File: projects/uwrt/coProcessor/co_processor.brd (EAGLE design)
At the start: 101.6 x 101.6 mm, 64 parts, among them U1 MPU-9250, U3 HTU21D

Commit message: No frills processing board revision 1.0.0
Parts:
- removed C1, C2: 0.1uF, rcl:C025-025X050
- removed C3: 10nF, rcl:C025-025X050
- removed C4: 100uF, rcl:C025-025X050
- removed C5: 4.7uF, rcl:C025-025X050
- removed C6: 100nF, rcl:C025-025X050
- removed JTAG_HEADER: M05X2-50MIL_SHROUD, Connectors:M05X2-50MIL-SHROUD
- removed U$2: LPS25H, st-microelectronics:LPS25H
- removed U$3: 24AA02, microchip:SO-08M
- removed U1: MPU-9250, SparkFun-Sensors:QFN24-3X3
- removed U3: HTU21D, SparkFun-Sensors:DFN-6-3X3-HTU21D
- added HB_R, HB_R1: 330, SparkFun-Resistors:0603
- added JTAG: (no value), pinhead:2X10
- added MICROSD: MICRO-SD_CARD_SOCKET, SparkFun-Connectors:MICRO-SD-SOCKET
- added MINI_USB_B: USB_MINI-B_SMT, SparkFun-Connectors:USB-MINIB
- added OSC1_C: 1nF, capacitor-wima:C2.5-2
- added OSC2_C: 1 nF, capacitor-wima:C2.5-2
- added Q1: (no value), crystal:HC49/S
- added RESET_SWITCH: (no value), switch-omron:B3F-10XX
- added STATUS_1, STATUS_2: (no value), SparkFun-LED:LED-1206
- added SWITCHES: 39-30-1040, molex:5569-04A2
- moved C15 300.6 mm to (70.6, 30.2), turned to 270 degrees
- moved C14 286.5 mm to (66.7, 30.2), turned to 270 degrees
- moved PWM_R9 278.5 mm to (72.2, 95.2), turned to 90 degrees
- moved PWM_LED9 275.8 mm to (70.6, 97.6), turned to 90 degrees
- moved C13 272.5 mm to (62.7, 30.2), turned to 270 degrees
- moved PWM_R8 269.0 mm to (68.3, 95.2), turned to 90 degrees
- moved PWM_LED8 266.3 mm to (66.7, 97.6), turned to 90 degrees
- moved PWM_R7 259.5 mm to (64.3, 95.2), turned to 90 degrees
- moved C12 258.5 mm to (58.7, 30.2), turned to 270 degrees
- moved PWM_LED7 256.8 mm to (62.7, 97.6), turned to 90 degrees
- moved PWM_R6 250.1 mm to (60.3, 95.2), turned to 90 degrees
- moved PWM_LED6 247.4 mm to (58.7, 97.6), turned to 90 degrees
- moved C11 244.4 mm to (54.8, 30.2), turned to 270 degrees
- moved PWM_R5 240.6 mm to (56.4, 95.2), turned to 90 degrees
- moved PWM_LED5 237.9 mm to (54.8, 97.6), turned to 90 degrees
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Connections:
- removed net GND1: JTAG_HEADER.3, JTAG_HEADER.5, JTAG_HEADER.9
- removed net N$6: U1.18, U1.20
- removed net N$9: C1.1, U1.10
- removed net TCK: JTAG_HEADER.4
- removed net TMS: JTAG_HEADER.2
- removed net VCC: JTAG_HEADER.1
- new net GND_ESC: PWM.1, PWM1.1, PWM2.1, PWM3.1, PWM4.1, PWM5.1, PWM6.1, PWM7.1, PWM8.1, PWM9.1, PWM_LED.C, PWM_LED1.C, PWM_LED2.C, PWM_LED3.C, PWM_LED4.C, PWM_LED5.C, PWM_LED6.C, PWM_LED7.C, PWM_LED8.C, PWM_LED9.C
- new net HB_OUT: HB_R.1, STM32F405.38
- new net HB_OUT1: HB_R1.1, STM32F405.37
- new net JTAG_RST: JTAG.3, STM32F405.56
- new net JTAG_TCK: JTAG.9, STM32F405.49
- new net JTAG_TDI: JTAG.5, STM32F405.50
- new net JTAG_TDO: JTAG.13, STM32F405.55
- new net JTAG_TMS: JTAG.7, STM32F405.46
- new net KILL_SW: STM32F405.34, SWITCHES.3
- new net N$3: HB_R1.2, STATUS_2.A
- new net NRST: JTAG.15, RESET_SWITCH.3, RESET_SWITCH.4, STM32F405.7
- new net OSC_IN: OSC1_C.2, Q1.1, STM32F405.5
- new net OSC_OUT: OSC2_C.2, Q1.2, STM32F405.6
- new net SDIO_CK: MICROSD.SCLK, STM32F405.53
- new net SDIO_CMD: MICROSD.CS, STM32F405.54
- new net SDIO_D0: MICROSD.DO, STM32F405.39
- new net START_SW: STM32F405.33, SWITCHES.4
- new net USB_DM: MINI_USB_B.D-, STM32F405.36
- new net USB_DP: MINI_USB_B.D+, STM32F405.35
- net +3V3: now also C11.1, JTAG.1, JTAG.2, MICROSD.VCC, MINI_USB_B.VBUS, SWITCHES.1, SWITCHES.2; no longer C2.1, C3.1, C4.1, C5.1, C6.1, U$2.1, U$2.10, U1.1, U1.13, U1.8, U3.VDD
- net GND: now also JTAG.10, JTAG.12, JTAG.14, JTAG.16, JTAG.18, JTAG.20, JTAG.4, JTAG.6, JTAG.8, MICROSD.CD1, MICROSD.CD2, MICROSD.GND, MICROSD.GND1, MICROSD.GND3, MINI_USB_B.GND, MINI_USB_B.S1, MINI_USB_B.S2, MINI_USB_B.S3, MINI_USB_B.S4, OSC1_C.1, OSC2_C.1, RESET_SWITCH.2, STATUS_1.C, STATUS_2.C; no longer C1.2, C11.1, C2.2, C3.2, C4.2, C5.2, C6.2, PWM_LED.C, PWM_LED1.C, PWM_LED2.C, PWM_LED3.C, PWM_LED4.C, PWM_LED5.C, PWM_LED6.C, PWM_LED7.C, PWM_LED8.C, PWM_LED9.C, U$2.3, U$2.8, U$2.9, U$3.4, U3.7, U3.GND
- net N$2: now also HB_R.2, STATUS_1.A; no longer JTAG_HEADER.10
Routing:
- net +3V3: track 29.6 -> 312.3 mm, vias 2 -> 5
- net GND: track 132.5 -> 221.2 mm, vias 3 -> 8
- net NRST: track 0.00 -> 83.3 mm, vias 0 -> 1
- net SDIO_D0: track 0.00 -> 80.6 mm, vias 0 -> 2
- net SDIO_CMD: track 0.00 -> 70.2 mm, vias 0 -> 2
- net JTAG_TMS: track 0.00 -> 63.4 mm
- net SDIO_CK: track 0.00 -> 61.9 mm, vias 0 -> 2
- net JTAG_TDI: track 0.00 -> 52.2 mm
- net JTAG_TCK: track 0.00 -> 52.1 mm, vias 0 -> 1
- net USB_DM: track 0.00 -> 51.1 mm
- net JTAG_RST: track 0.00 -> 50.7 mm
- net JTAG_TDO: track 0.00 -> 50.5 mm, vias 0 -> 1
- net USB_DP: track 0.00 -> 49.3 mm
- net I2C_SDA: track 0.00 -> 45.7 mm, vias 0 -> 1
- net I2C_SCL: track 0.00 -> 42.7 mm, vias 0 -> 1
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- added copper zone on layer 16, net GND_ESC

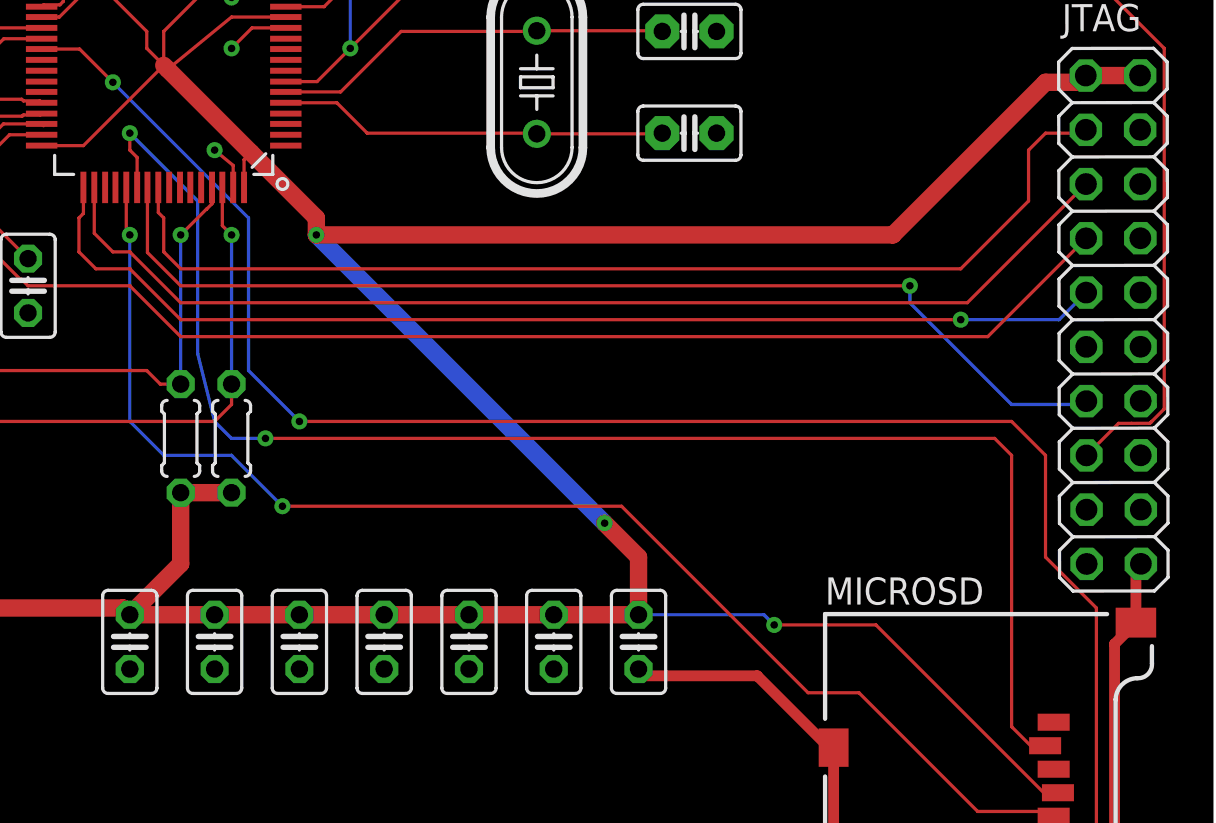
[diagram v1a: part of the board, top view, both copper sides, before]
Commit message: Minor touchups, fixed fragmenting GND plane
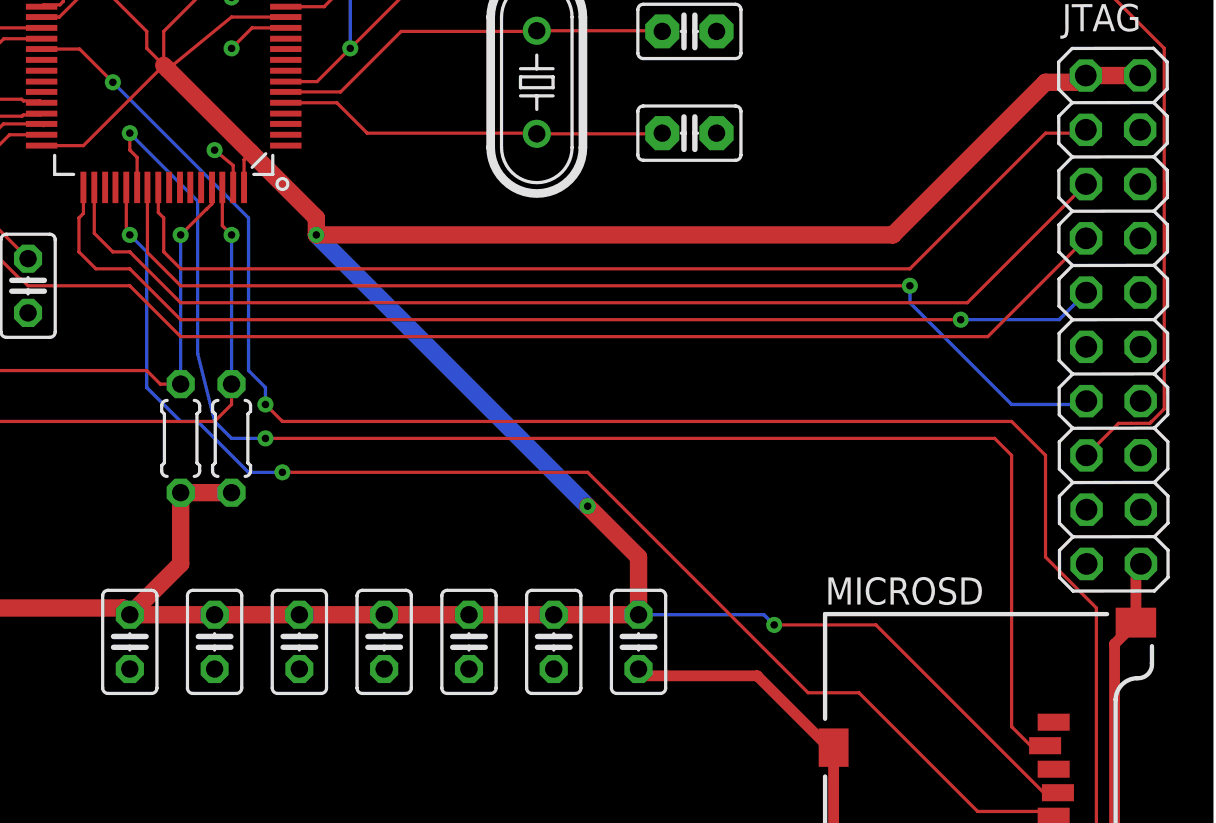
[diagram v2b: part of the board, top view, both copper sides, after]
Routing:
- net SDIO_CK: track 61.9 -> 60.5 mm
- net JTAG_RST: track 50.7 -> 49.4 mm
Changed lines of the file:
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@@
 <wire x1="53.18125" y1="33.81375" x2="50.8" y2="31.4325" width="0.8128" layer="1"/>
 <wire x1="74.6125" y1="31.4325" x2="74.6125" y2="34.13125" width="0.8128" layer="1"/>
-<wire x1="74.6125" y1="34.13125" x2="73.025" y2="35.71875" width="0.8128" layer="1"/>
-<via x="73.025" y="35.71875" extent="1-16" drill="0.35"/>
+<wire x1="74.6125" y1="34.13125" x2="72.23125" y2="36.5125" width="0.8128" layer="1"/>
+<via x="72.23125" y="36.5125" extent="1-16" drill="0.35"/>
 <via x="59.53125" y="49.2125" extent="1-16" drill="0.35"/>
-<wire x1="73.025" y1="35.71875" x2="59.53125" y2="49.2125" width="0.8128" layer="16"/>
+<wire x1="72.23125" y1="36.5125" x2="59.53125" y2="49.2125" width="0.8128" layer="16"/>
 <wire x1="59.53125" y1="50.00625" x2="59.53125" y2="49.2125" width="0.8128" layer="1"/>
 <wire x1="56.473703125" y1="53.063796875" x2="59.53125" y2="50.00625" width="0.8128" layer="1"/>
@@
 <wire x1="52.3875" y1="50.00625" x2="52.3875" y2="48.41875" width="0.1524" layer="1"/>
 <wire x1="52.3875" y1="48.41875" x2="53.18125" y2="47.625" width="0.1524" layer="1"/>
-<wire x1="53.18125" y1="47.625" x2="89.69375" y2="47.625" width="0.1524" layer="1"/>
-<wire x1="89.69375" y1="47.625" x2="92.86875" y2="50.8" width="0.1524" layer="1"/>
-<wire x1="92.86875" y1="50.8" x2="92.86875" y2="53.18125" width="0.1524" layer="1"/>
-<wire x1="92.86875" y1="53.18125" x2="93.6625" y2="53.975" width="0.1524" layer="1"/>
+<wire x1="95.4397625" y1="54.019296875" x2="95.395465625" y2="53.975" width="0.1524" layer="1"/>
+<wire x1="95.4397625" y1="54.019296875" x2="95.551984375" y2="54.13151875" width="0.1524" layer="1"/>
+<wire x1="53.18125" y1="47.625" x2="87.3125" y2="47.625" width="0.1524" layer="1"/>
+<wire x1="87.3125" y1="47.625" x2="93.6625" y2="53.975" width="0.1524" layer="1"/>
 <wire x1="93.6625" y1="53.975" x2="95.395465625" y2="53.975" width="0.1524" layer="1"/>
-<wire x1="95.395465625" y1="53.975" x2="95.551984375" y2="54.13151875" width="0.1524" layer="1"/>
+<wire x1="95.395465625" y1="53.975" x2="95.4397625" y2="54.019296875" width="0.1524" layer="1"/>
 </signal>
 <signal name="JTAG_TMS">
@@
 <wire x1="46.6725" y1="57.912" x2="48.4505" y2="57.912" width="0.1524" layer="1"/>
 <wire x1="48.4505" y1="57.912" x2="50.00625" y2="56.35625" width="0.1524" layer="1"/>
-<via x="58.7375" y="40.48125" extent="1-16" drill="0.35"/>
-<wire x1="58.7375" y1="40.48125" x2="92.075" y2="40.48125" width="0.1524" layer="1"/>
-<wire x1="92.075" y1="40.48125" x2="93.6625" y2="38.89375" width="0.1524" layer="1"/>
+<via x="57.15" y="41.275" extent="1-16" drill="0.35"/>
+<wire x1="93.6625" y1="38.89375" x2="92.075" y2="40.48125" width="0.1524" layer="1"/>
 <wire x1="93.6625" y1="38.89375" x2="93.6625" y2="34.13125" width="0.1524" layer="1"/>
 <wire x1="93.6625" y1="34.13125" x2="96.04375" y2="31.75" width="0.1524" layer="1"/>
@@
 <wire x1="95.25" y1="19.84375" x2="94.085" y2="19.84375" width="0.1524" layer="1"/>
 <wire x1="94.085" y1="19.84375" x2="94.04375" y2="19.8025" width="0.1524" layer="1"/>
-<wire x1="56.35625" y1="42.8625" x2="56.35625" y2="50.00625" width="0.1524" layer="16"/>
-<wire x1="58.7375" y1="40.48125" x2="56.35625" y2="42.8625" width="0.1524" layer="16"/>
+<wire x1="56.35625" y1="50.00625" x2="56.35625" y2="42.8625" width="0.1524" layer="16"/>
 <wire x1="56.35625" y1="50.00625" x2="50.00625" y2="56.35625" width="0.1524" layer="16"/>
+<wire x1="56.35625" y1="42.8625" x2="57.15" y2="42.06875" width="0.1524" layer="16"/>
+<wire x1="57.15" y1="42.06875" x2="57.15" y2="41.275" width="0.1524" layer="16"/>
+<wire x1="92.075" y1="40.48125" x2="57.94375" y2="40.48125" width="0.1524" layer="1"/>
+<wire x1="57.94375" y1="40.48125" x2="57.15" y2="41.275" width="0.1524" layer="1"/>
 </signal>
 <signal name="SDIO_CK">
@@
 <wire x1="50.6349" y1="51.435" x2="50.6349" y2="49.3776" width="0.1524" layer="1"/>
 <wire x1="50.6349" y1="49.3776" x2="50.8" y2="49.2125" width="0.1524" layer="1"/>
-<wire x1="50.8" y1="49.2125" x2="50.8" y2="40.48125" width="0.1524" layer="16"/>
-<wire x1="50.8" y1="40.48125" x2="52.3875" y2="38.89375" width="0.1524" layer="16"/>
-<wire x1="52.3875" y1="38.89375" x2="55.5625" y2="38.89375" width="0.1524" layer="16"/>
-<wire x1="55.5625" y1="38.89375" x2="57.94375" y2="36.5125" width="0.1524" layer="16"/>
-<via x="57.94375" y="36.5125" extent="1-16" drill="0.35"/>
-<wire x1="57.94375" y1="36.5125" x2="73.81875" y2="36.5125" width="0.1524" layer="1"/>
-<wire x1="82.55" y1="27.78125" x2="84.93125" y2="27.78125" width="0.1524" layer="1"/>
+<via x="57.94375" y="38.1" extent="1-16" drill="0.35"/>
+<wire x1="84.93125" y1="27.78125" x2="82.55" y2="27.78125" width="0.1524" layer="1"/>
 <wire x1="84.93125" y1="27.78125" x2="90.4875" y2="22.225" width="0.1524" layer="1"/>
 <wire x1="90.4875" y1="22.225" x2="93.82125" y2="22.225" width="0.1524" layer="1"/>
 <wire x1="93.82125" y1="22.225" x2="94.04375" y2="22.0025" width="0.1524" layer="1"/>
-<wire x1="73.81875" y1="36.5125" x2="82.55" y2="27.78125" width="0.1524" layer="1"/>
+<wire x1="53.975" y1="40.48125" x2="53.18125" y2="40.48125" width="0.1524" layer="16"/>
+<wire x1="53.18125" y1="40.48125" x2="51.59375" y2="42.06875" width="0.1524" layer="16"/>
+<wire x1="51.59375" y1="42.06875" x2="51.59375" y2="48.41875" width="0.1524" layer="16"/>
+<wire x1="51.59375" y1="48.41875" x2="50.8" y2="49.2125" width="0.1524" layer="16"/>
+<wire x1="57.94375" y1="38.1" x2="56.35625" y2="38.1" width="0.1524" layer="16"/>
+<wire x1="56.35625" y1="38.1" x2="53.975" y2="40.48125" width="0.1524" layer="16"/>
+<wire x1="72.23125" y1="38.1" x2="57.94375" y2="38.1" width="0.1524" layer="1"/>
+<wire x1="82.55" y1="27.78125" x2="72.23125" y2="38.1" width="0.1524" layer="1"/>
 </signal>
 <signal name="SDIO_CMD">
